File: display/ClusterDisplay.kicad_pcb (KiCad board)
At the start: 4 copper layers, 104.8 x 106 mm, 76 parts, among them J1 Verdin iMX95 Hexa 8GB WB IT, J10 RTC coin cell, J2 Power in, J3 CAN to ECU, J4 DM-TFTR50-413 panel, J8 JTAG debug, J9 Buttons, Q1 PMV55ENEA (AEC-Q101, 60V/20V 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, Q2 PMV55ENEA (AEC-Q101, 60V/20V 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, Q3 MFT6N2A5S23A (AEC-Q101, 60V/2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, U1 LM74930-Q1, U2 LM61460-Q1, U3 TLV767-Q1, U4 TCAN1044V-Q1, U6 TPS60403-Q1, U7 AL8853AQ

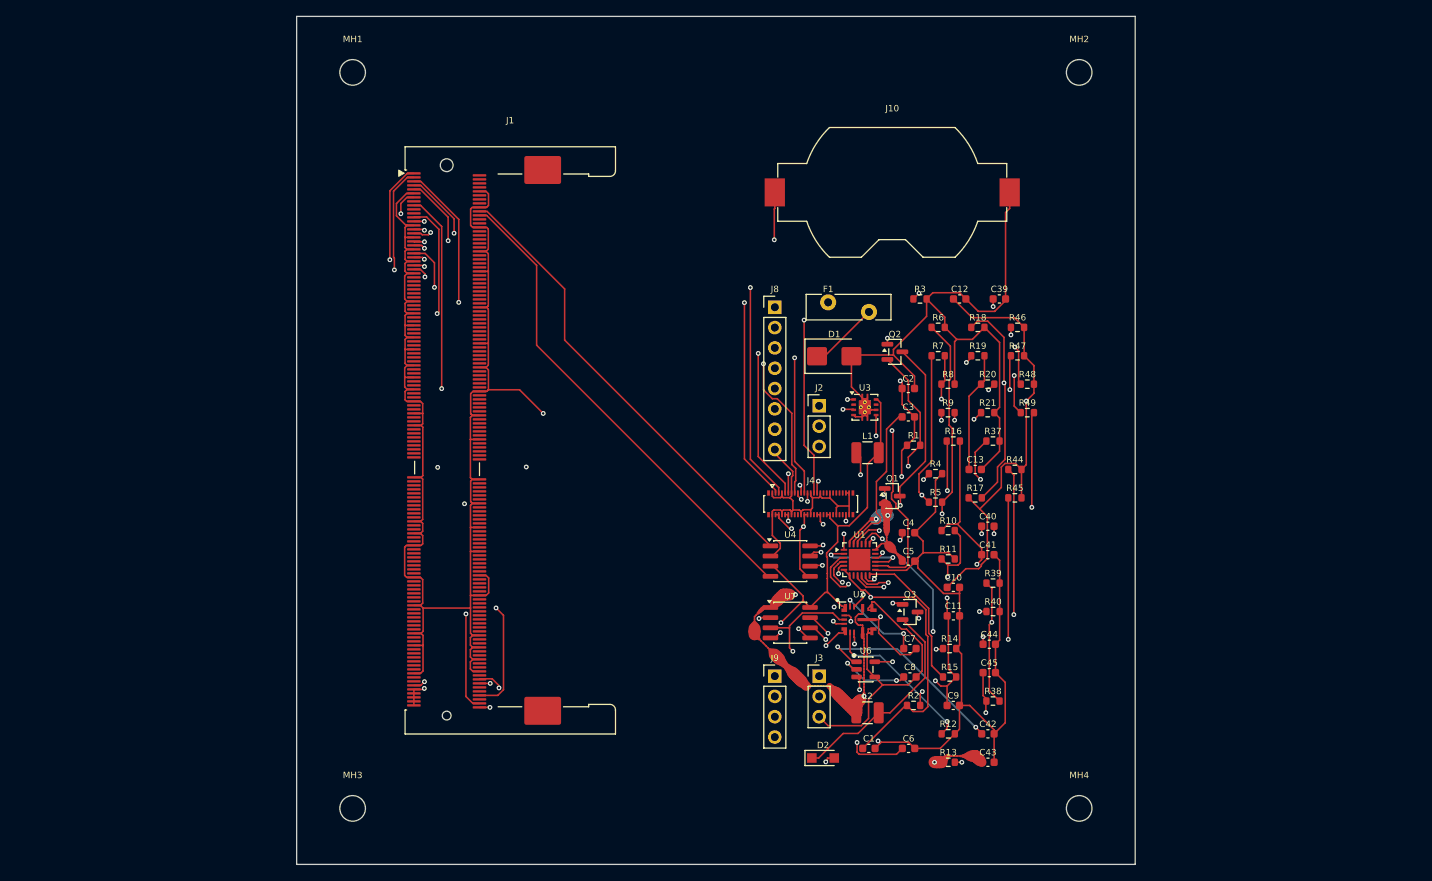
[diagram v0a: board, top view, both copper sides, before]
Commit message: display: switch to the 800-nit TSD TST040HDBC-42 round panel
The 350-nit DM-TFTR50-413 washes out in sun, is rated only -20..60C, and its
127mm circle would be cropped by the 105.5mm dash opening. New panel: 4in,
800 nits, -30..80C, 101.5mm active circle. Adds TPS65131-Q1 +/-6.5V rails,
TPS61165-Q1 15V/180mA backlight with PWM dimming, Hirose FH26 FPC connector,
real harness connectors J2/J3/J8/J9, and open solder jumpers for the panel's
datasheet-conflicting +/-6.5V pin polarity. Re-routed (0 unconnected), BOM
regenerated. Also adds the website dashboard graphic under media/.

Co-Authored-By: Claude Sonnet 5.5 <noreply@anthropic.com>
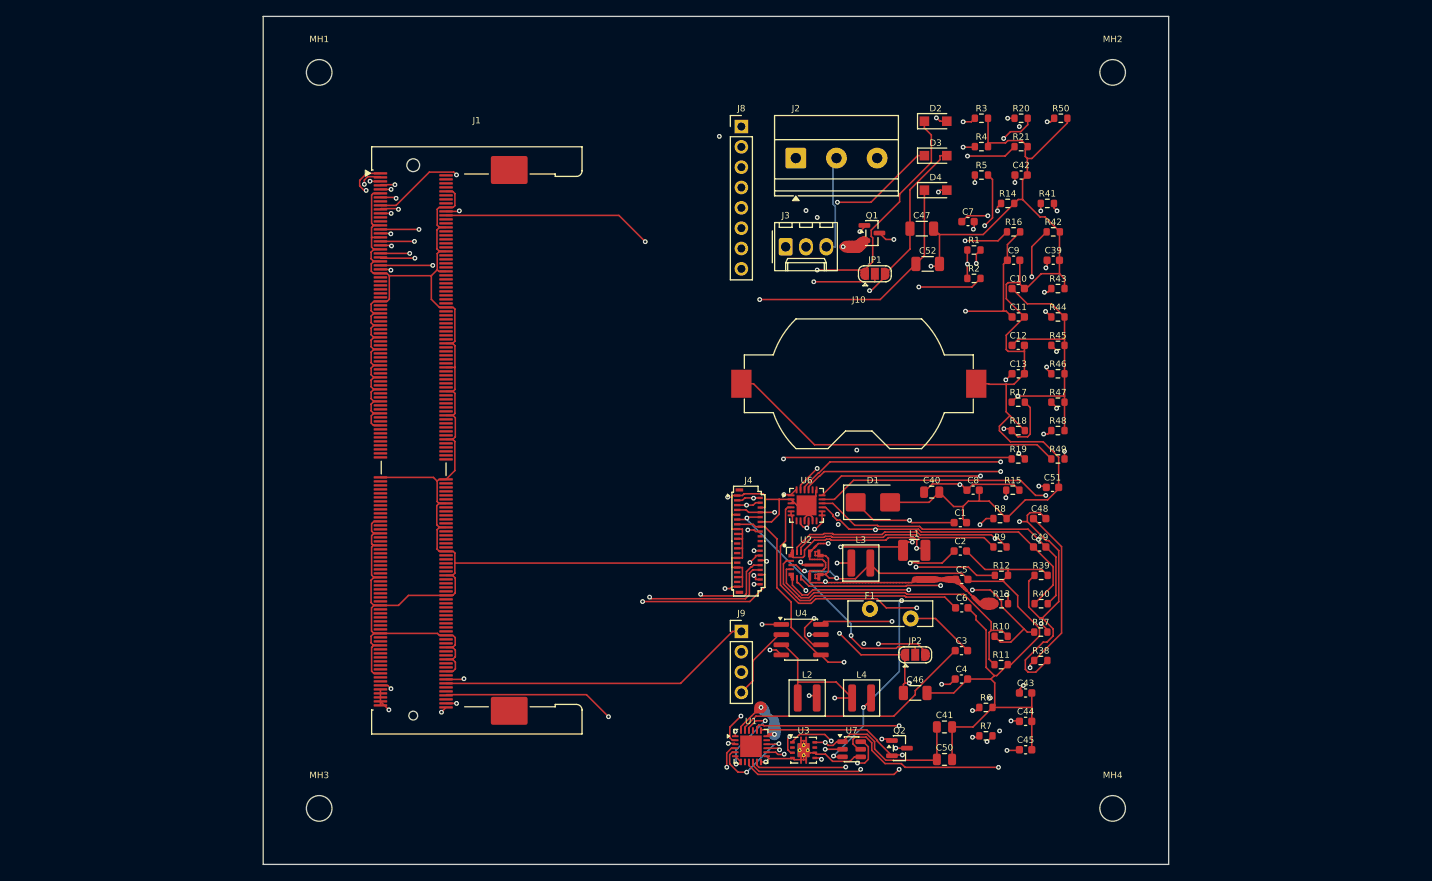
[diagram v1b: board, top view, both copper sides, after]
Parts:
- removed Q3: MFT6N2A5S23A (AEC-Q101, 60V/2.5A), Package_TO_SOT_SMD:SOT-23
- added C46: 22u VPOS out 16V (AEC-Q200), Capacitor_SMD:C_1206_3216Metric, F.Cu at (234.9, 180.1)
- added C47: 22u VNEG out 16V (AEC-Q200), Capacitor_SMD:C_1206_3216Metric, F.Cu at (235.7, 122.0)
- added C48: 12p VPOS feed-forward (AEC-Q200), Capacitor_SMD:C_0603_1608Metric, F.Cu at (250.5, 158.3)
- added C49: 15p VNEG feed-forward (AEC-Q200), Capacitor_SMD:C_0603_1608Metric, F.Cu at (250.5, 161.8)
- added C50: 10u BL input (AEC-Q200), Capacitor_SMD:C_0805_2012Metric, F.Cu at (238.6, 188.4)
- added C51: 220n BL COMP (AEC-Q200), Capacitor_SMD:C_0603_1608Metric, F.Cu at (252.1, 154.4)
- added C52: 10u BL output 25V (AEC-Q200), Capacitor_SMD:C_1206_3216Metric, F.Cu at (236.5, 126.4)
- added D3: PMEG6010ELRX (AEC-Q101, 60V/1A), Diode_SMD:Nexperia_CFP3_SOD-123W, F.Cu at (237.5, 112.9)
- added D4: PMEG6010ELRX (AEC-Q101, 60V/1A), Diode_SMD:Nexperia_CFP3_SOD-123W, F.Cu at (237.5, 117.2)
- added JP1: SJ3 OPEN: bridge 1-2 if datasheet TABLE is right (7-8=+6.5V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, Jumper:SolderJumper-3_P1.3mm_Open_RoundedPad1.0x1.5mm, F.Cu at (229.9, 127.7)
- added JP2: SJ3 OPEN: bridge 2-3 if datasheet TABLE is right (10-11=-6.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, Jumper:SolderJumper-3_P1.3mm_Open_RoundedPad1.0x1.5mm, F.Cu at (234.9, 175.3)
- added L3: 4.7u inverter (Coilcraft XAL4030-472ME), Inductor_SMD:L_Coilcraft_XAL4030-XXX, F.Cu at (228.1, 163.8)
- added L4: 10u BL boost (Coilcraft XAL4040-103ME), Inductor_SMD:L_Coilcraft_XAL4040-XXX, F.Cu at (228.2, 180.7)
- added R41: 100k VNEG bottom R4 to VREF (see docstring), Resistor_SMD:R_0603_1608Metric, F.Cu at (251.4, 118.9)
- added R42: 1.10R LED current sense (0.2V/1.10=182mA), Resistor_SMD:R_0603_1608Metric, F.Cu at (252.2, 122.4)
- added R43: 100k bias-enable pulldown, Resistor_SMD:R_0603_1608Metric, F.Cu at (252.8, 129.5)
- added R50: 100k panel-reset pulldown, Resistor_SMD:R_0603_1608Metric, F.Cu at (253.1, 108.2)
- C40: value 1u Cfly (AEC-Q200) -> 4.7u boost in (AEC-Q200); footprint Capacitor_SMD:C_0603_1608Metric -> Capacitor_SMD:C_0805_2012Metric
- C41: value 1u CI (AEC-Q200) -> 4.7u inverter in (AEC-Q200); footprint Capacitor_SMD:C_0603_1608Metric -> Capacitor_SMD:C_0805_2012Metric
- C42: value 1u CO (AEC-Q200) -> 100n VIN filter (AEC-Q200)
- C43: value 1u VIN (AEC-Q200) -> 220n VREF (AEC-Q200)
- C44: value 10n COMP (typical, not loop-verified) -> 10n CP comp (AEC-Q200)
- C45: value 1u VOUT, 63V-rated (AEC-Q200) -> 4n7 CN comp (AEC-Q200)
- J2: value Power in -> Phoenix MKDS 1,5/3-5,08 power in (DTM06-3S pigtail); footprint Connector_PinHeader_2.54mm:PinHeader_1x03_P2.54mm_Vertical -> TerminalBlock_Phoenix:TerminalBlock_Phoenix_MKDS-1,5-3-5.08_1x03_P5.08mm_Horizontal
- J3: value CAN to ECU -> Molex KK-254 22-27-2031 CAN (DTM06-3S pigtail); footprint Connector_PinHeader_2.54mm:PinHeader_1x03_P2.54mm_Vertical -> Connector_Molex:Molex_KK-254_AE-6410-03A_1x03_P2.54mm_Vertical
- J4: value DM-TFTR50-413 panel -> TST040HDBC-42 panel; footprint Connector_Hirose_DF40:Hirose_DF40C-50DP-0.4V_2x25-1MP_P0.4mm -> Connector_FFC-FPC:Hirose_FH26-39S-0.3SHW_2Rows-39Pins-1MP_P0.60mm_Horizontal
- J8: value JTAG debug -> Samtec TSW-108-07-G-S JTAG (bench only)
- J9: value Buttons -> Samtec TSW-104-07-G-S buttons (bench only)
- L2: value 680u boost inductor (real, see docstring math) -> 4.7u boost (Coilcraft XAL4030-472ME); footprint Inductor_SMD:L_1210_3225Metric -> Inductor_SMD:L_Coilcraft_XAL4030-XXX
- R37: value 2.00R OCP/CS sense (real, see docstring math) -> 100R VIN filter
- R38: value 232k OVP top (real, see docstring math) -> 562k VPOS top R1 (see docstring)
- R39: value 10k OVP bottom (real, see docstring math) -> 130k VPOS bottom R2 (see docstring)
- R40: value 10.0R LED FB (real, see docstring math) -> 536k VNEG top R3 (see docstring)
- U6: value TPS60403-Q1 -> TPS65131-Q1; footprint Package_TO_SOT_SMD:SOT-23-5 -> Package_DFN_QFN:HVQFN-24-1EP_4x4mm_P0.5mm_EP2.5x2.5mm
- U7: value AL8853AQ -> TPS61165-Q1; footprint Package_SO:SOIC-8_3.9x4.9mm_P1.27mm -> Package_TO_SOT_SMD:SOT-23-6
- moved D2 80.8 mm to (237.5, 108.6)
- moved C42 70.0 mm to (248.2, 115.3)
- moved C9 56.2 mm to (247.2, 126.0)
- moved R14 56.1 mm to (246.5, 118.9)
- moved R2 53.9 mm to (242.2, 128.2)
- moved C7 53.9 mm to (241.5, 121.2)
- moved J3 53.8 mm to (218.7, 124.3)
- moved Q2 49.5 mm to (232.9, 187.0)
- moved R7 47.9 mm to (243.8, 185.4)
- moved R6 47.9 mm to (243.8, 181.9)
- moved U3 43.5 mm to (221.0, 187.2)
- moved R5 41.3 mm to (243.2, 115.3)
- moved R4 41.3 mm to (243.2, 111.8)
- moved F1 38.7 mm to (229.2, 169.6)
- moved C11 38.2 mm to (247.8, 133.1)
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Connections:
- C40 pad 1: VSN_CFLY_P -> +5V
- C40 pad 2: VSN_CFLY_N -> GND
- C42 pad 1: PANEL_VSN_NEG5V -> PANEL_BIAS_VIN
- C43 pad 1: +12V_PROT -> PANEL_VREF
- C44 pad 1: BL_COMP -> PANEL_CP
- C45 pad 1: PANEL_BL_LEDA_38V -> PANEL_CN
- D2 pad 1: BL_SW -> PANEL_VSP
- D2 pad 2: PANEL_BL_LEDA_38V -> PANEL_BOOST_SW
- J1 pad 19: (no net) -> PANEL_BL_PWM
- J1 pad 21: (no net) -> PANEL_BIAS_EN
- J1 pad 23: DSI_D3_N -> (no net)
- J1 pad 25: DSI_D3_P -> (no net)
- J4 pad 10: PANEL_BL_LEDA_38V -> PANEL_PIN_B
- J4 pad 11: DSI_D1_N -> PANEL_PIN_B
- J4 pad 12: PANEL_BL_LEDA_38V -> GND
- J4 pad 13: GND -> +1V8
- J4 pad 14: GND -> +1V8
- J4 pad 15: DSI_CLK_P -> GND
- J4 pad 16: (no net) -> DSI_PANEL_EN
- J4 pad 17: DSI_CLK_N -> GND
- J4 pad 2: GND -> PANEL_BL_LEDA
- J4 pad 20: GND -> (no net)
- J4 pad 21: DSI_D0_P -> (no net)
- J4 pad 22: +1V8 -> (no net)
- J4 pad 23: DSI_D0_N -> GND
- J4 pad 24: +1V8 -> DSI_D2_P
- J4 pad 25: GND -> (no net)
- J4 pad 26: GND -> DSI_D2_N
- J4 pad 27: DSI_D3_P -> GND
- J4 pad 28: (no net) -> DSI_CLK_P
- J4 pad 29: DSI_D3_N -> (no net)
- J4 pad 3: DSI_D2_P -> PANEL_BL_LEDA
- J4 pad 30: PANEL_VSN_NEG5V -> DSI_CLK_N
- J4 pad 32: PANEL_VSN_NEG5V -> DSI_D1_P
- J4 pad 34: (no net) -> DSI_D1_N
- J4 pad 35: (no net) -> GND
- J4 pad 36: +5V -> DSI_D0_P
- J4 pad 37: GND -> (no net)
- J4 pad 38: +5V -> DSI_D0_N
- J4 pad 39: (no net) -> GND
- J4 pad 5: DSI_D2_N -> PANEL_BL_LEDK
- J4 pad 6: PANEL_BL_LEDK -> GND
- J4 pad 7: GND -> PANEL_PIN_A
- J4 pad 8: GND -> PANEL_PIN_A
- J4 pad 9: DSI_D1_P -> GND
- L2 pad 1: +12V_PROT -> +5V
- L2 pad 2: BL_SW -> PANEL_BOOST_SW
- R37 pad 1: BL_CS_NODE -> +5V
- R37 pad 2: GND -> PANEL_BIAS_VIN
- R38 pad 1: PANEL_BL_LEDA_38V -> PANEL_VSP
- R38 pad 2: BL_OVP_DIV -> PANEL_FBP
- R39 pad 1: BL_OVP_DIV -> PANEL_FBP
- R40 pad 1: PANEL_BL_LEDK -> PANEL_VSN
- R40 pad 2: GND -> PANEL_FBN
- U6 pad 1: PANEL_VSN_NEG5V -> PANEL_BOOST_SW
- U6 pad 2: +5V -> GND
- U6 pad 3: VSN_CFLY_N -> GND
- U6 pad 4: GND -> PANEL_BIAS_VIN
- U6 pad 5: VSN_CFLY_P -> +5V
- U7 pad 1: +12V_PROT -> +5V
- U7 pad 2: BL_GATE -> PANEL_BL_PWM
- U7 pad 3: GND -> BL_SW
- U7 pad 4: BL_CS_NODE -> GND
- U7 pad 5: PANEL_BL_LEDK -> BL_COMP
- U7 pad 6: BL_COMP -> PANEL_BL_LEDK
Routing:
- net PANEL_VSP: track 0.00 -> 133.2 mm, vias 0 -> 5
- net PANEL_BIAS_EN: track 0.00 -> 131.2 mm, vias 0 -> 4
- net PANEL_VSN: track 0.00 -> 111.0 mm, vias 0 -> 3
- net PANEL_BIAS_VIN: track 0.00 -> 104.4 mm, vias 0 -> 3
- net PANEL_BL_PWM: track 0.00 -> 99.4 mm, vias 0 -> 2
- net PANEL_VREF: track 0.00 -> 94.2 mm, vias 0 -> 3
- net PANEL_BOOST_SW: track 0.00 -> 91.7 mm, vias 0 -> 4
- net GND: track 576.8 -> 658.9 mm, vias 4 -> 5
- net PANEL_FBN: track 0.00 -> 80.9 mm, vias 0 -> 2
- net IMON: track 20.1 -> 99.1 mm
- net +5V: track 166.7 -> 244.8 mm
- net DSI_D3_P: track 76.0 -> 0.00 mm, vias 2 -> 0
- net PANEL_FBP: track 0.00 -> 72.6 mm, vias 0 -> 2
- net DSI_D3_N: track 72.3 -> 0.00 mm, vias 2 -> 0
- net DGATE: track 9.80 -> 75.6 mm, vias 2 -> 3
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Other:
- board size 104.8 x 106 mm -> 113.2 x 106 mm

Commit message: display rev B: ignition-wake circuit on the Verdin WAKE1 pin, re-routed
IGN -> 56k -> clamped divider (BAV99-Q to GND/+5V) -> PMV55ENEA pulling
IGN_WAKE_N low, 10k pull-up to +1V8, onto CTRL_WAKE1_MICO# (X1 252). ERC now
0 violations, routed 0 unconnected, BOM regenerated.

Co-Authored-By: Claude Sonnet 5.5 <noreply@anthropic.com>
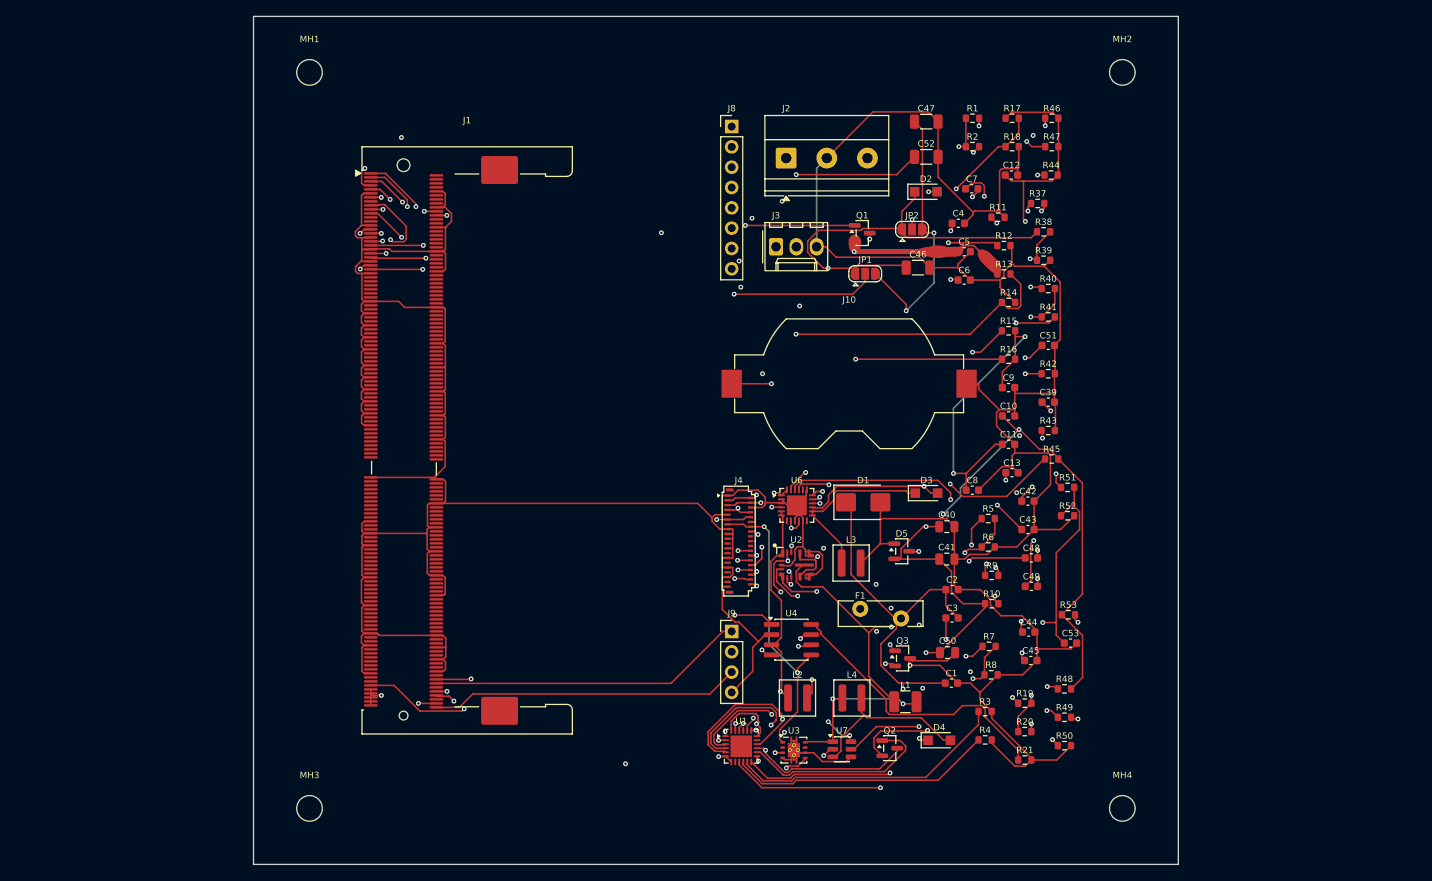
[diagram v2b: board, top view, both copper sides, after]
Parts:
- added C53: 10n ignition filter, Capacitor_SMD:C_0603_1608Metric, F.Cu at (254.3, 173.8)
- added D5: BAV99-Q ignition clamp (AEC-Q101), Package_TO_SOT_SMD:SOT-23, F.Cu at (233.2, 162.4)
- added Q3: PMV55ENEA ignition wake pulldown, Package_TO_SOT_SMD:SOT-23, F.Cu at (233.3, 175.8)
- added R51: 56k ignition series, Resistor_SMD:R_0603_1608Metric, F.Cu at (254.0, 154.4)
- added R52: 33k ignition divider bottom, Resistor_SMD:R_0603_1608Metric, F.Cu at (254.0, 157.9)
- added R53: 10k wake pull-up to +1V8, Resistor_SMD:R_0603_1608Metric, F.Cu at (254.1, 170.3)
- J3: value Molex KK-254 22-27-2031 CAN (DTM06-3S pigtail) -> Molex KK-254 22-27-2031 private CAN link to gauges/ J8
- moved R50 78.4 mm to (253.6, 186.7)
- moved R20 76.7 mm to (248.6, 184.9)
- moved R21 76.7 mm to (248.6, 188.4)
- moved R4 74.2 mm to (243.7, 185.9)
- moved R3 74.2 mm to (243.7, 182.4)
- moved D4 68.8 mm to (237.9, 186.0)
- moved C4 57.0 mm to (240.3, 121.4)
- moved R11 55.9 mm to (245.3, 120.6)
- moved R37 53.6 mm to (250.2, 118.9)
- moved R38 53.6 mm to (251.0, 122.4)
- moved JP2 53.2 mm to (234.5, 122.1)
- moved C46 53.2 mm to (235.3, 126.9)
- moved R5 42.9 mm to (244.0, 158.3)
- moved D3 42.2 mm to (236.3, 155.1)
- moved R12 41.2 mm to (246.0, 124.2)
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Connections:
- J1 pad 252: (no net) -> IGN_WAKE_N
- J2 pad 3: (no net) -> IGN_SENSE
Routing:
- net IGN_WAKE_N: track 0.00 -> 87.0 mm, vias 0 -> 4
- net IGN_SENSE: track 0.00 -> 69.2 mm, vias 0 -> 1
- net IMON: track 99.1 -> 33.0 mm, vias 2 -> 0
- net ILIM: track 100.3 -> 34.6 mm, vias 2 -> 0
- net RESET_MOCI: track 94.8 -> 157.4 mm, vias 2 -> 3
- net IGN_GATE: track 0.00 -> 61.0 mm, vias 0 -> 4
- net TMR: track 34.7 -> 94.2 mm
- net BL_SW: track 79.8 -> 21.4 mm, vias 4 -> 0
- net PANEL_BL_LEDA: track 59.4 -> 111.5 mm, vias 2 -> 4
- net SW_SENSE: track 107.3 -> 59.3 mm
- net +1V8: track 124.9 -> 171.4 mm, vias 4 -> 5
- net PANEL_INV_SW: track 65.2 -> 22.5 mm, vias 3 -> 0
- net OV_DIV: track 108.2 -> 66.0 mm, vias 5 -> 3
- net CAN1_STB: track 77.8 -> 36.2 mm, vias 2 -> 0
- net FB_5V: track 38.6 -> 79.8 mm, vias 0 -> 3
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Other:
- board size 113.2 x 106 mm -> 115.6 x 106 mm
